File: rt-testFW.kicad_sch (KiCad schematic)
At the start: 13 parts, among them J1 1Min, J2 2Min, J3 3Min, J4 5Min, SW1 TestStart-Peach, SW2 Reset-Black

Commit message: initial iteration complete
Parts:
- removed D1: LED, LED_THT:LED_D4.0mm, symbol Device:LED
- removed J1: 1Min, Connector_PinSocket_2.54mm:PinSocket_1x02_P2.54mm_Vertical, symbol Connector:Conn_01x02_Socket
- removed J2: 2Min, Connector_PinSocket_2.54mm:PinSocket_1x02_P2.54mm_Vertical, symbol Connector:Conn_01x02_Socket
- removed J3: 3Min, Connector_PinSocket_2.54mm:PinSocket_1x02_P2.54mm_Vertical, symbol Connector:Conn_01x02_Socket
- removed J4: 5Min, Connector_PinSocket_2.54mm:PinSocket_1x02_P2.54mm_Vertical, symbol Connector:Conn_01x02_Socket
- removed R2, R3, R4, R5: R, Resistor_THT:R_Axial_DIN0309_L9.0mm_D3.2mm_P2.54mm_Vertical, symbol Device:R
- removed SW1: TestStart-Peach, Button_Switch_THT:SW_PUSH_6mm, symbol Switch:SW_Push_Dual
- removed SW2: Reset-Black, Button_Switch_THT:SW_PUSH_6mm, symbol Switch:SW_Push_Dual
- added J1-1Min1, J2-2Min1, J3-3Min1, J4-5Min1, J5-CLK-DIO1, J5-VCC-GND1: Conn_01x02_Male, Connector_PinHeader_2.00mm:PinHeader_1x02_P2.00mm_Vertical, symbol Connector:Conn_01x02_Male
- added LED1: LED, Connector_PinHeader_2.00mm:PinHeader_1x02_P2.00mm_Vertical, symbol Device:LED
- added Reset-Black1, TestStart-Peach1: SW_Push_Dual, Button_Switch_THT:SW_PUSH_6mm, symbol Switch:SW_Push_Dual
- R1: footprint Resistor_THT:R_Axial_DIN0309_L9.0mm_D3.2mm_P2.54mm_Vertical -> Connector_PinHeader_2.00mm:PinHeader_1x02_P2.00mm_Vertical
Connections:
- net at R1.1: now also LED1.2 (A)
- net at A1.23 (D8): now also J3-3Min1.1 (Pin_1)
- net at A1.17 (D2): now also J1-1Min1.1 (Pin_1)
- net at A1.22 (D7): now also J2-2Min1.1 (Pin_1)
- net at A1.21 (D6): now also TestStart-Peach1.1
- net at A1.27 (D12): now also J4-5Min1.1 (Pin_1)
- net at A1.18 (D3): now also J5-CLK-DIO1.1 (Pin_1)
- net at A1.20 (D5): now also J5-CLK-DIO1.2 (Pin_2)
- net at A1.29 (GND): now also LED1.1 (K), TestStart-Peach1.2
- net at A1.3 (~{RESET}): now also Reset-Black1.1
- net at A1.5 (+5V): now also J1-1Min1.2 (Pin_2), J2-2Min1.2 (Pin_2), J3-3Min1.2 (Pin_2), J4-5Min1.2 (Pin_2), J5-VCC-GND1.1 (Pin_1)
- net at A1.7 (GND): now also J5-VCC-GND1.2 (Pin_2), Reset-Black1.2

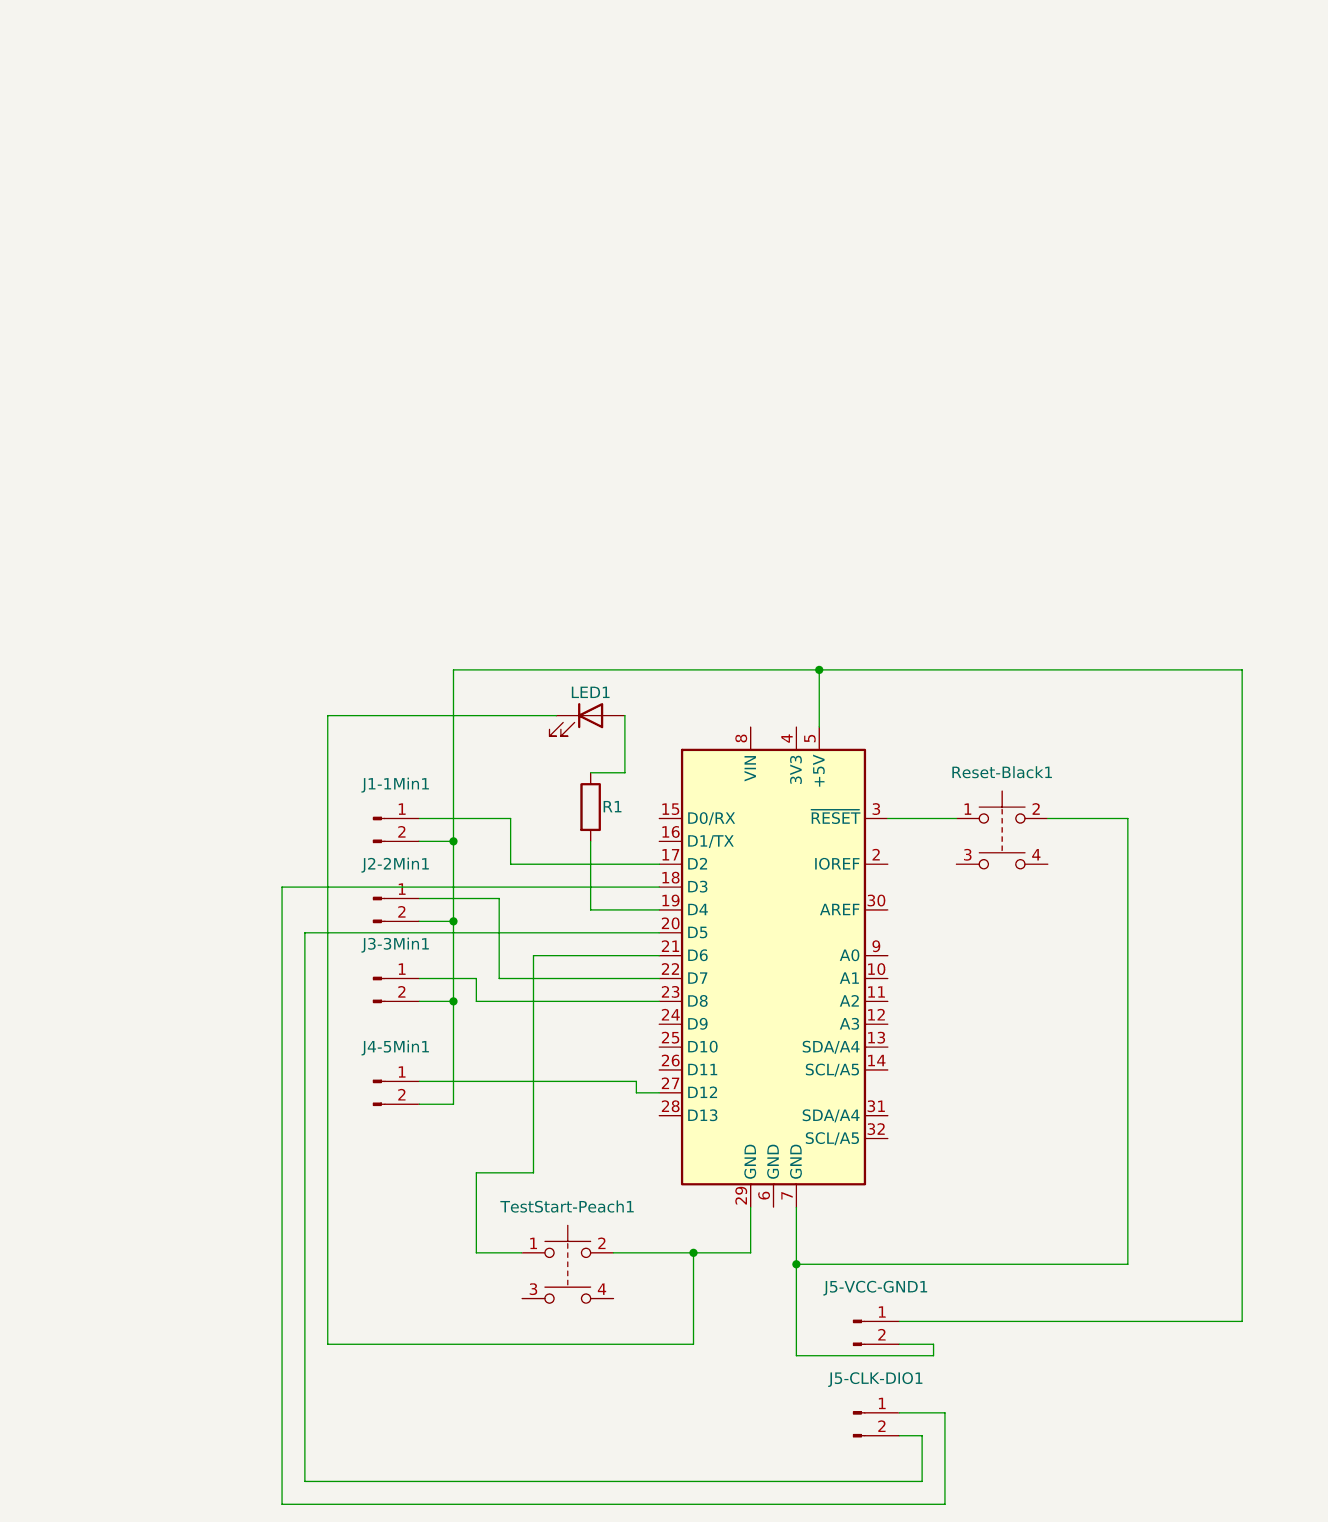
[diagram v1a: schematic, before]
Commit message: final update to support tm1637 digital output
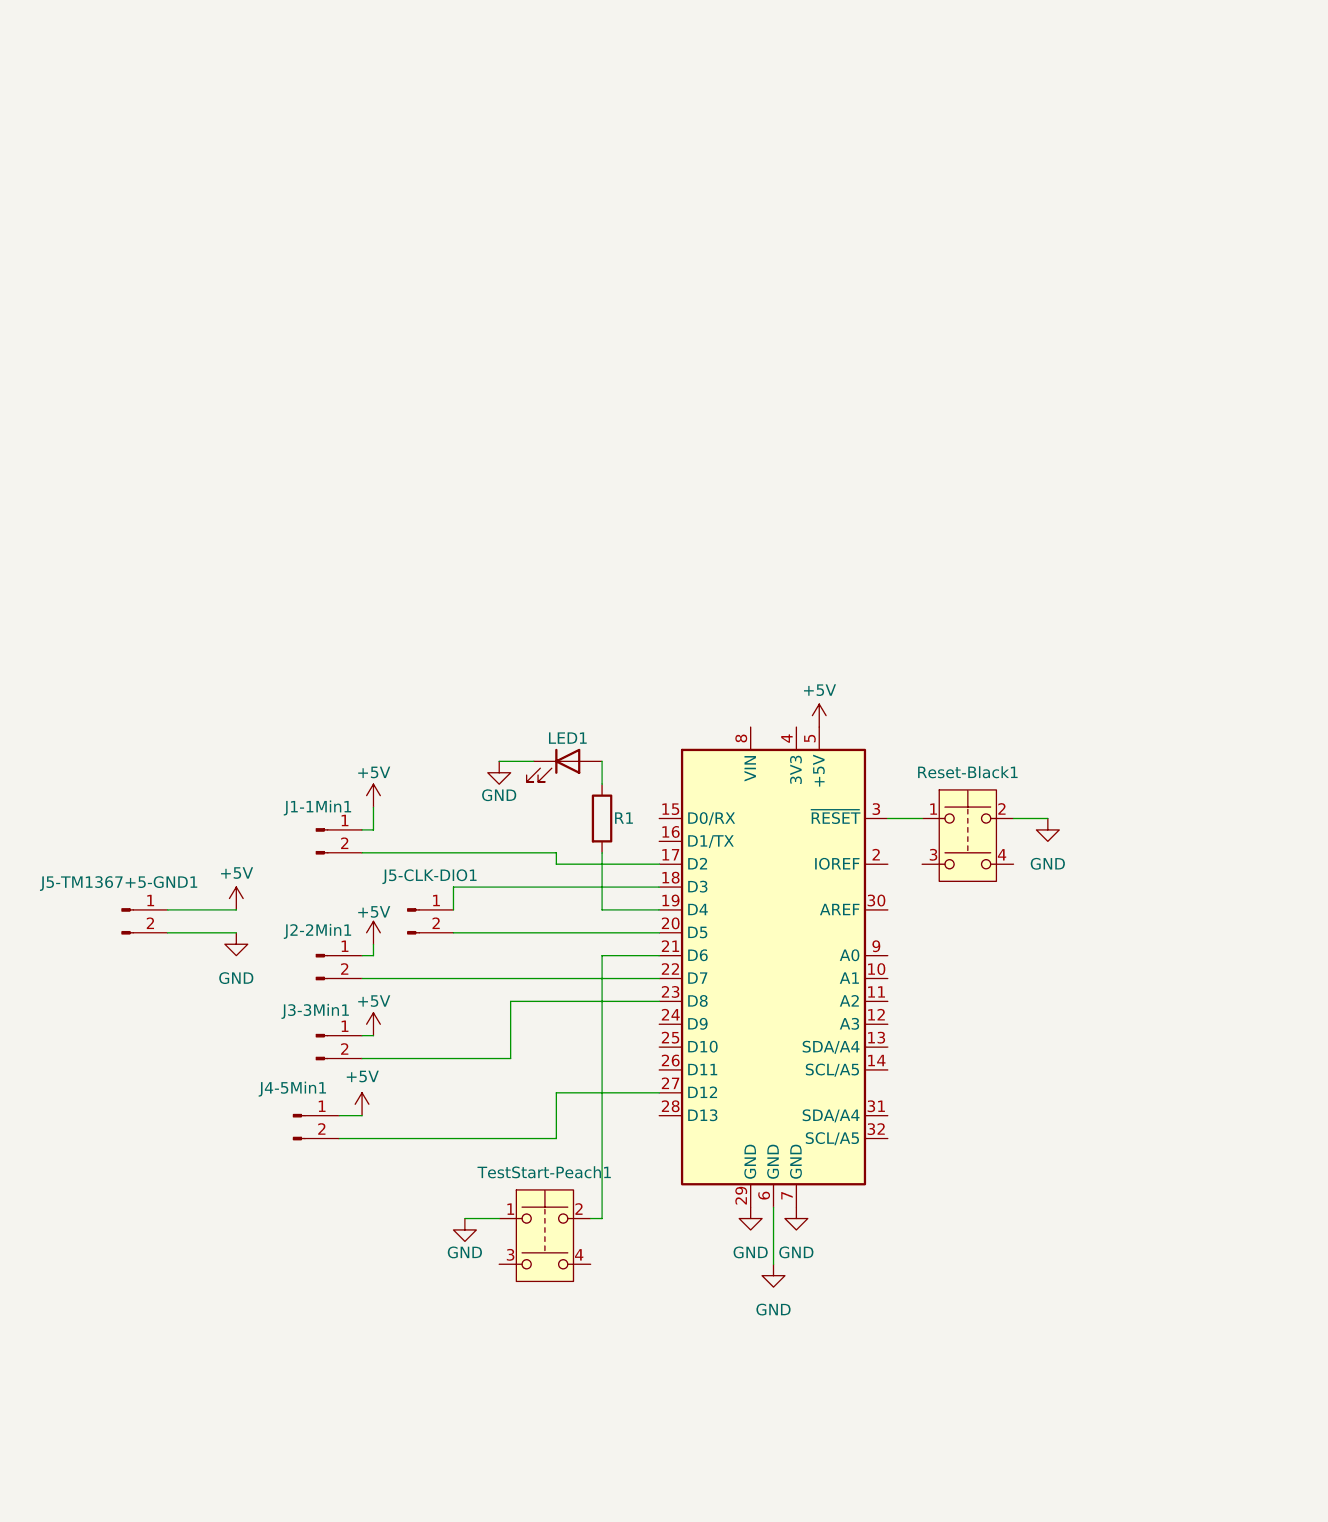
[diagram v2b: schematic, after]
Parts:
- J1-1Min1, J2-2Min1, J3-3Min1, J4-5Min1, J5-CLK-DIO1: footprint Connector_PinHeader_2.00mm:PinHeader_1x02_P2.00mm_Vertical -> Connector_PinSocket_2.54mm:PinSocket_1x02_P2.54mm_Vertical
- J5-TM1367+5-GND1: renamed from J5-VCC-GND1; footprint Connector_PinHeader_2.00mm:PinHeader_1x02_P2.00mm_Vertical -> Connector_PinSocket_2.54mm:PinSocket_1x02_P2.54mm_Vertical
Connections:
- net at A1.21 (D6): now also TestStart-Peach1.2; no longer TestStart-Peach1.1
- net GND: now reaches A1.29 (GND), LED1.1 (K)
- net GND: now also A1.6 (GND), A1.7 (GND), J5-TM1367+5-GND1.2 (Pin_2), Reset-Black1.2, TestStart-Peach1.1; no longer TestStart-Peach1.2
- net at A1.23 (D8): now also J3-3Min1.2 (Pin_2); no longer J3-3Min1.1 (Pin_1)
- net at A1.22 (D7): now also J2-2Min1.2 (Pin_2); no longer J2-2Min1.1 (Pin_1)
- net at A1.27 (D12): now also J4-5Min1.2 (Pin_2); no longer J4-5Min1.1 (Pin_1)
- net at A1.17 (D2): now also J1-1Min1.2 (Pin_2); no longer J1-1Min1.1 (Pin_1)
- new net +5V: A1.5 (+5V), J1-1Min1.1 (Pin_1), J2-2Min1.1 (Pin_1), J3-3Min1.1 (Pin_1), J4-5Min1.1 (Pin_1), J5-TM1367+5-GND1.1 (Pin_1)
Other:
- moved on the sheet: J1-1Min1, J2-2Min1, J3-3Min1, J4-5Min1, J5-CLK-DIO1, J5-TM1367+5-GND1, LED1, R1

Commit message: pcb-flip complete, add custom uno library
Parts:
- A1: footprint Module:Arduino_UNO_R3 -> KiCad-Library:Arduino_UNO_R3
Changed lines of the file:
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@@
 			)
 		)
-		(property "Footprint" "Module:Arduino_UNO_R3"
+		(property "Footprint" "KiCad-Library:Arduino_UNO_R3"
 			(at 148.59 119.38 0)
 			(effects

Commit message: partial commit to save work
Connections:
- net +5V: no longer J1-1Min1.1 (Pin_1), J2-2Min1.1 (Pin_1), J3-3Min1.1 (Pin_1), J4-5Min1.1 (Pin_1)
- net GND: now also J1-1Min1.1 (Pin_1), J2-2Min1.1 (Pin_1), J3-3Min1.1 (Pin_1), J4-5Min1.1 (Pin_1)
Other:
- moved on the sheet: J3-3Min1, J4-5Min1
